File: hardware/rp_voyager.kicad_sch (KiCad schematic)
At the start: 0 parts

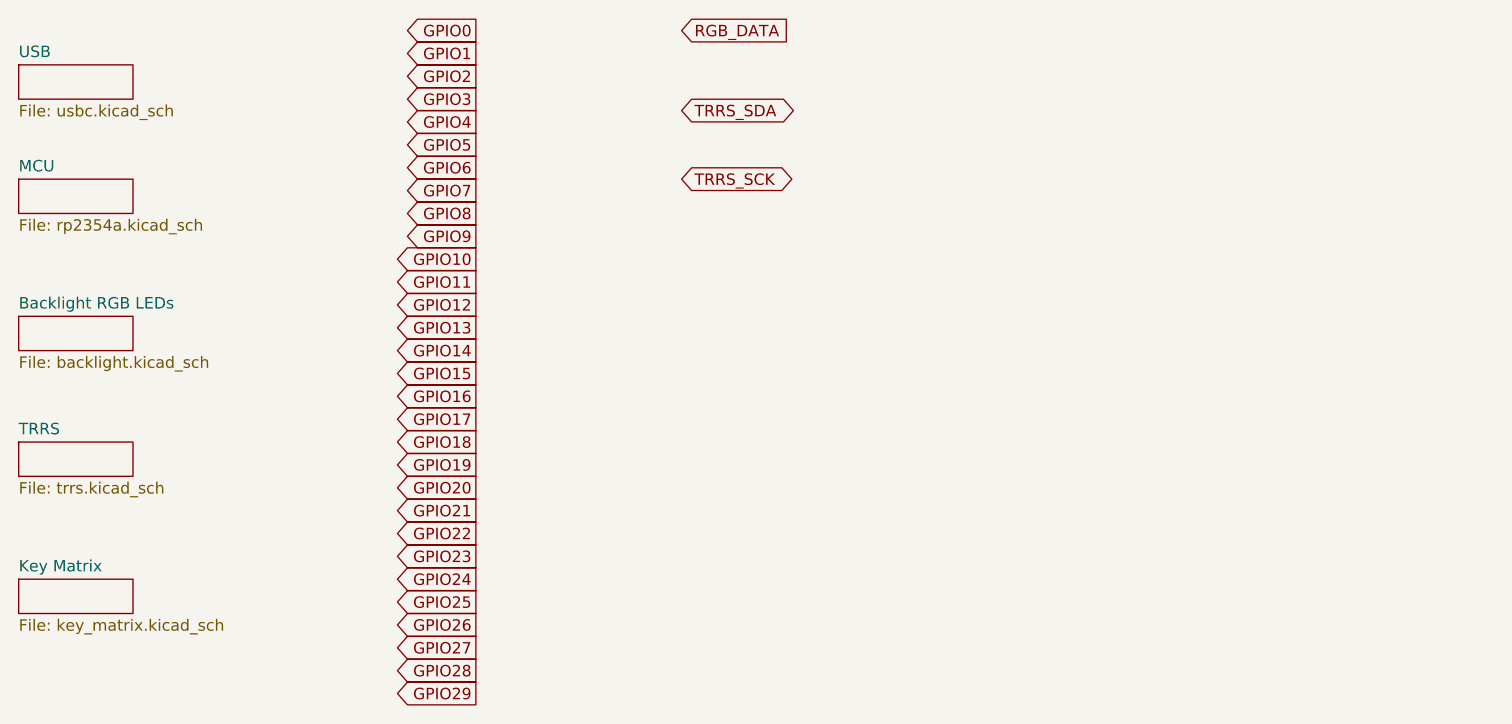
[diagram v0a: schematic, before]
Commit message: separate left/right part design, schematic
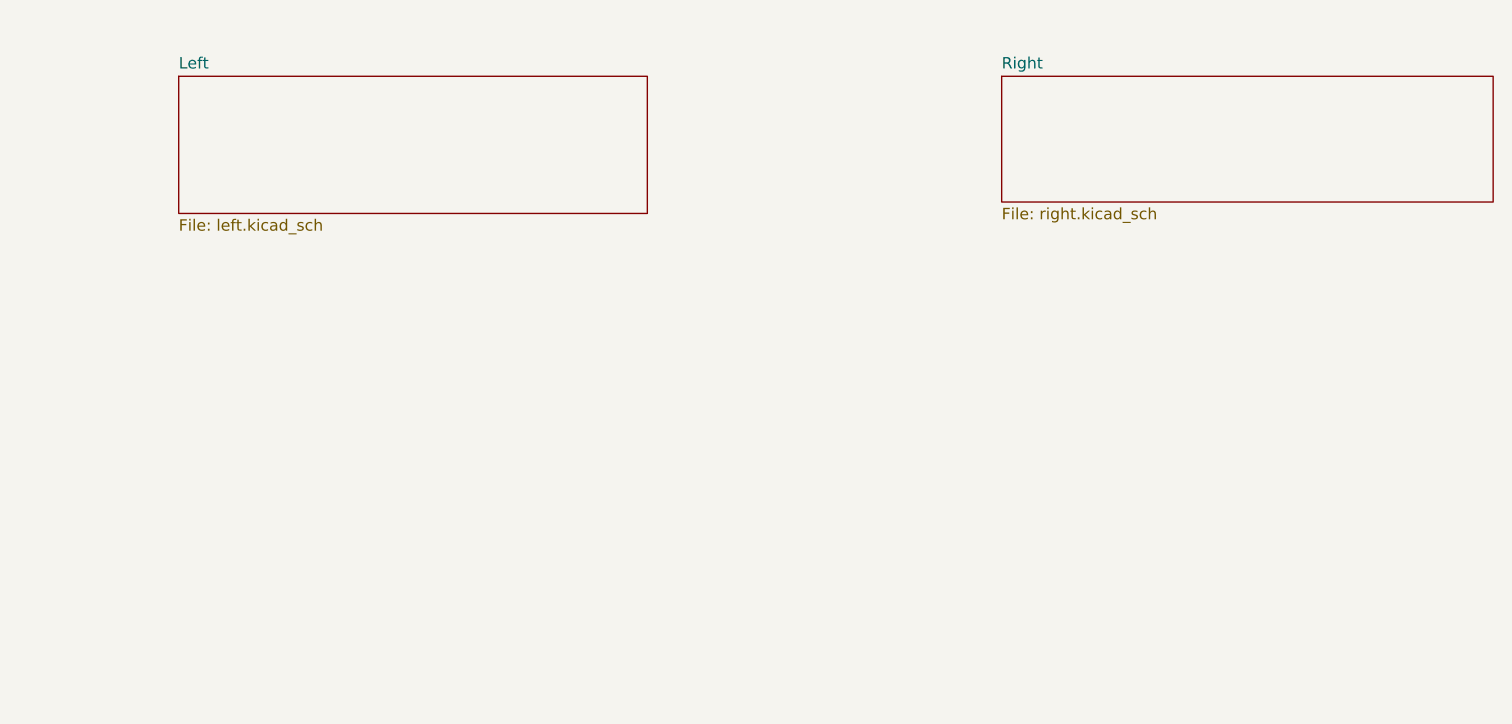
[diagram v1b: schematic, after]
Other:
- removed sheet Backlight RGB LEDs
- removed sheet Key Matrix
- removed sheet MCU
- removed sheet TRRS
- removed sheet USB
- added sheet Left (left.kicad_sch)
- added sheet Right (right.kicad_sch)
